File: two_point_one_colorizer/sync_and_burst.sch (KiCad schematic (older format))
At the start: 12 parts, among them J5 Conn_01x03, U4 LM1881, U5 74HC86, U6 4013

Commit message: update circuits
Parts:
- added R?: 1.5k, Resistor_THT:R_Axial_DIN0207_L6.3mm_D2.5mm_P7.62mm_Horizontal, symbol Device:R
- R10: value 10k -> 1k
- R14: value 12k -> 1.5k
- R9: value 1k -> 10k
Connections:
- net GND: now also R?.1; no longer R10.1
- new net black_and_sync: R10.1, R?.2
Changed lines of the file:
@@
 P 9200 5325
 F 0 "R14" H 9270 5371 50  0000 L CNN
-F 1 "12k" H 9270 5280 50  0000 L CNN
+F 1 "1.5k" H 9270 5280 50  0000 L CNN
 F 2 "Resistor_THT:R_Axial_DIN0207_L6.3mm_D2.5mm_P7.62mm_Horizontal" V 9130 5325 50  0001 C CNN
 F 3 "~" H 9200 5325 50  0001 C CNN
@@
 P 6075 1500
 F 0 "R9" H 5950 1500 50  0000 C CNN
-F 1 "1k" H 5900 1600 50  0000 C CNN
+F 1 "10k" H 5900 1600 50  0000 C CNN
 F 2 "Resistor_THT:R_Axial_DIN0207_L6.3mm_D2.5mm_P7.62mm_Horizontal" V 6005 1500 50  0001 C CNN
 F 3 "~" H 6075 1500 50  0001 C CNN
@@
 P 6575 1800
 F 0 "R10" V 6368 1800 50  0000 C CNN
-F 1 "10k" V 6459 1800 50  0000 C CNN
+F 1 "1k" V 6459 1800 50  0000 C CNN
 F 2 "Resistor_THT:R_Axial_DIN0207_L6.3mm_D2.5mm_P7.62mm_Horizontal" V 6505 1800 50  0001 C CNN
 F 3 "~" H 6575 1800 50  0001 C CNN
@@
 L power:GND #PWR?
 U 1 1 5F2CD17D
-P 6800 1950
+P 7225 1950
 AR Path="/5F2CD17D" Ref="#PWR?"  Part="1"
 AR Path="/5F1CF562/5F2CD17D" Ref="#PWR030"  Part="1"
-F 0 "#PWR030" H 6800 1700 50  0001 C CNN
-F 1 "GND" H 6805 1777 50  0000 C CNN
-F 2 "" H 6800 1950 50  0001 C CNN
-F 3 "" H 6800 1950 50  0001 C CNN
-	1    6800 1950
+F 0 "#PWR030" H 7225 1700 50  0001 C CNN
+F 1 "GND" H 7230 1777 50  0000 C CNN
+F 2 "" H 7225 1950 50  0001 C CNN
+F 3 "" H 7225 1950 50  0001 C CNN
+	1    7225 1950
 	1    0    0    -1
 $EndComp
@@
 	5025 1800 6075 1800
 Connection ~ 6075 1800
+$Comp
+L Device:R R?
+U 1 1 5F549749
+P 6950 1950
+F 0 "R?" V 6850 1950 50  0000 C CNN
+F 1 "1.5k" V 7050 1950 50  0000 C CNN
+F 2 "Resistor_THT:R_Axial_DIN0207_L6.3mm_D2.5mm_P7.62mm_Horizontal" V 6880 1950 50  0001 C CNN
+F 3 "~" H 6950 1950 50  0001 C CNN
+	1    6950 1950
+	0    1    1    0
+$EndComp
+Wire Wire Line
+	7225 1950 7100 1950
 $EndSCHEMATC

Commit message: revised all boards
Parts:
- U6: value 4013 -> CD4013
- gave numbers to parts that had none: 1
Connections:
- net at U6.3 (C): now also R10.2, R9.1, U4.1 (CSYNC); no longer U4.3 (FRAME)
- no-connect marks 7 -> 8
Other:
- note added: "csync"
- note removed: "vsync"
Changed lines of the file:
@@
 P 4675 5525
 F 0 "U6" H 4900 6000 50  0000 C CNN
-F 1 "4013" H 4900 5900 50  0000 C CNN
+F 1 "CD4013" H 4900 5900 50  0000 C CNN
 F 2 "Package_DIP:DIP-14_W7.62mm_LongPads" H 4675 5525 50  0001 C CNN
 F 3 "http://www.onsemi.com/pub/Collateral/MC14013B-D.PDF" H 4675 5525 50  0001 C CNN
@@
 P 2200 7100
 F 0 "U6" H 2430 7146 50  0000 L CNN
-F 1 "4013" H 2430 7055 50  0000 L CNN
+F 1 "CD4013" H 2430 7055 50  0000 L CNN
 F 2 "Package_DIP:DIP-14_W7.62mm_LongPads" H 2200 7100 50  0001 C CNN
 F 3 "http://www.onsemi.com/pub/Collateral/MC14013B-D.PDF" H 2200 7100 50  0001 C CNN
@@
 	5075 4950 5075 5625
 Text Notes 3975 5450 0    50   ~ 0
-vsync
+csync
 $Comp
 L 4xxx:4013 U6
@@
 P 3325 7125
 F 0 "U6" H 3325 7606 50  0000 C CNN
-F 1 "4013" H 3325 7515 50  0000 C CNN
+F 1 "CD4013" H 3325 7515 50  0000 C CNN
 F 2 "Package_DIP:DIP-14_W7.62mm_LongPads" H 3325 7125 50  0001 C CNN
 F 3 "http://www.onsemi.com/pub/Collateral/MC14013B-D.PDF" H 3325 7125 50  0001 C CNN
@@
 	3725 3500 5400 3500
 Wire Wire Line
-	5400 3500 5400 2125
-Wire Wire Line
-	5400 2125 5025 2125
-Wire Wire Line
 	5025 2225 7650 2225
 Wire Wire Line
@@
 Connection ~ 6075 1800
 $Comp
-L Device:R R?
+L Device:R R35
 U 1 1 5F549749
 P 6950 1950
-F 0 "R?" V 6850 1950 50  0000 C CNN
+F 0 "R35" V 6850 1950 50  0000 C CNN
 F 1 "1.5k" V 7050 1950 50  0000 C CNN
 F 2 "Resistor_THT:R_Axial_DIN0207_L6.3mm_D2.5mm_P7.62mm_Horizontal" V 6880 1950 50  0001 C CNN
@@
 Wire Wire Line
 	7225 1950 7100 1950
+Wire Wire Line
+	5400 2025 5025 2025
+Wire Wire Line
+	5400 2025 5400 3500
+Connection ~ 5025 2025
+NoConn ~ 5025 2125
 $EndSCHEMATC

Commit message: working on nexr version for colorizer and inverter
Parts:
- removed J5: Conn_01x03, Connector_PinHeader_2.54mm:PinHeader_1x03_P2.54mm_Vertical, symbol Connector_Generic:Conn_01x03
- added C21: 0.1n, Capacitor_THT:C_Disc_D4.7mm_W2.5mm_P5.00mm, symbol Device:C_Small
- added R36: 10k, Resistor_THT:R_Axial_DIN0207_L6.3mm_D2.5mm_P7.62mm_Horizontal, symbol Device:R
- added RV9: 20k_pot, lib_fp:Potentiometer_Vertical_Large, symbol Device:R_POT
- added SW4: SPDT_slide, lib_fp:spdt_slide_switch_small_tayda, symbol Switch:SW_SPDT
- added U11: 74HC4538, Package_DIP:DIP-16_W7.62mm_LongPads, symbol symbol:74HC4538
- R35: value 1.5k -> 1k (or 1.2k maybe)
- U4: footprint Package_DIP:DIP-8_W7.62mm_LongPads -> lib_fp:DIP-SOIC-8
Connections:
- net +5V: now also R9.1, RV9.1, U11.16 (VDD), U11.3 (~CD); no longer R9.2, U6.6 (S)
- net GND: now also U6.6 (S), SW4.1 (A), U11.4 (B), U11.8 (VSS)
- net burst_pulse: now also U11.7 (~Q); no longer U4.5 (BURST)
- net at U6.1 (Q): now also SW4.3 (C)
- net at R10.2, U4.1 (CSYNC), U6.3 (C): now also R9.2, U11.5 (~A); no longer R9.1
- net at U5.10: now also SW4.2 (B)
- new net: C21.2, U11.1 (Cx)
- new net: C21.1, R36.2, U11.2 (RxCx)
- new net: R36.1, RV9.2
- no-connect marks 8 -> 18
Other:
- moved on the sheet: C12, C13, R10, R11, R12, R13, R14, R35, R9, U4, U5C, U6A

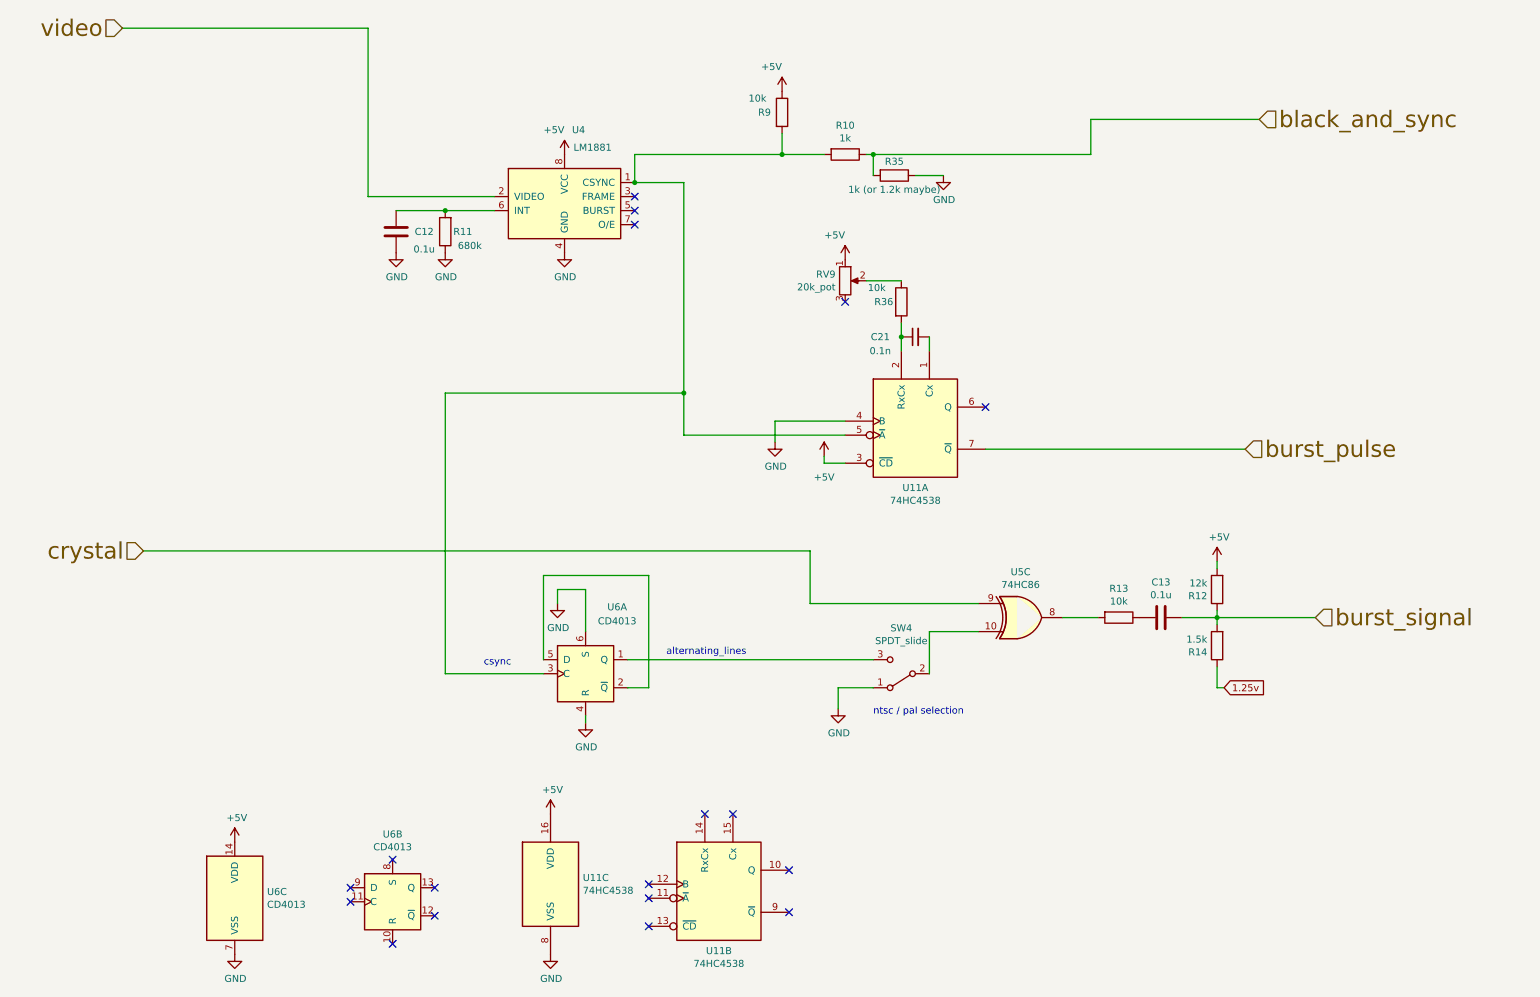
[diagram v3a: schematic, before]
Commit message: lay out colorizer
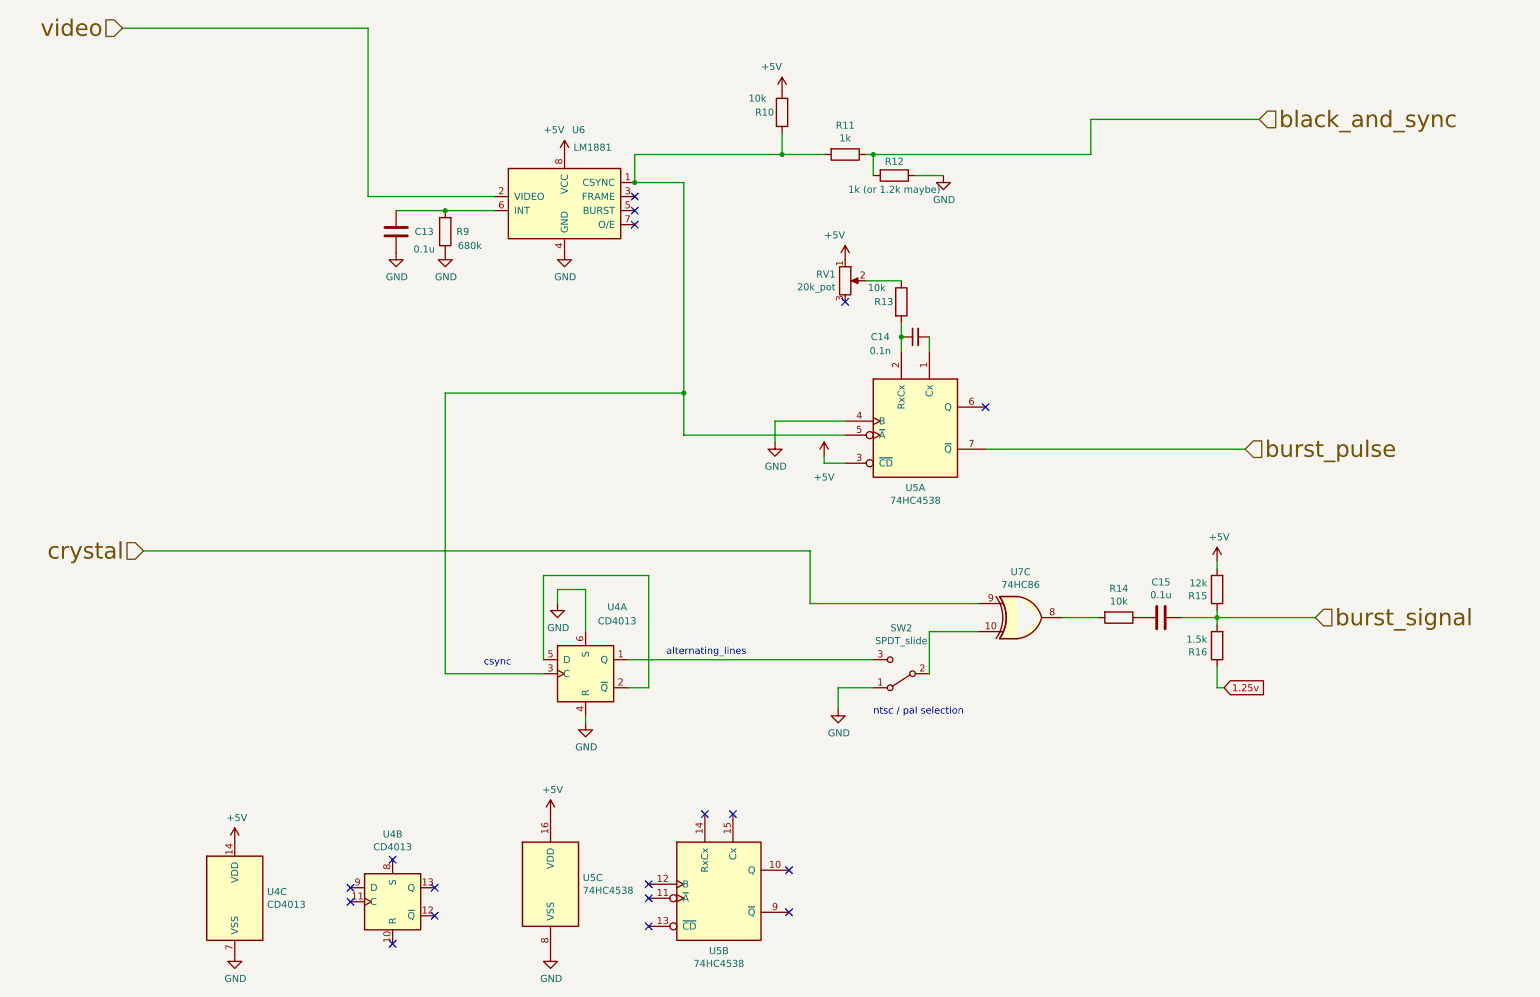
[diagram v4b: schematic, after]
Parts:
- C13: renamed from C12; footprint Capacitor_THT:C_Disc_D4.7mm_W2.5mm_P5.00mm -> lib_fp:C_Disc_D4.7mm_W2.5mm_P5.00mm
- C14: renamed from C21; footprint Capacitor_THT:C_Disc_D4.7mm_W2.5mm_P5.00mm -> lib_fp:C_Disc_D4.7mm_W2.5mm_P5.00mm
- C15: renamed from C13; footprint Capacitor_THT:C_Disc_D4.7mm_W2.5mm_P5.00mm -> lib_fp:C_Disc_D4.7mm_W2.5mm_P5.00mm
- R10: renamed from R9; footprint Resistor_THT:R_Axial_DIN0207_L6.3mm_D2.5mm_P7.62mm_Horizontal -> lib_fp:R_Axial_DIN0207_L6.3mm_D2.5mm_P7.62mm_Horizontal
- R11: renamed from R10; footprint Resistor_THT:R_Axial_DIN0207_L6.3mm_D2.5mm_P7.62mm_Horizontal -> lib_fp:R_Axial_DIN0207_L6.3mm_D2.5mm_P7.62mm_Horizontal
- R12: renamed from R35; footprint Resistor_THT:R_Axial_DIN0207_L6.3mm_D2.5mm_P7.62mm_Horizontal -> lib_fp:R_Axial_DIN0207_L6.3mm_D2.5mm_P7.62mm_Horizontal
- R13: renamed from R36; footprint Resistor_THT:R_Axial_DIN0207_L6.3mm_D2.5mm_P7.62mm_Horizontal -> lib_fp:R_Axial_DIN0207_L6.3mm_D2.5mm_P7.62mm_Horizontal
- R14: renamed from R13; footprint Resistor_THT:R_Axial_DIN0207_L6.3mm_D2.5mm_P7.62mm_Horizontal -> lib_fp:R_Axial_DIN0207_L6.3mm_D2.5mm_P7.62mm_Horizontal
- R15: renamed from R12; footprint Resistor_THT:R_Axial_DIN0207_L6.3mm_D2.5mm_P7.62mm_Horizontal -> lib_fp:R_Axial_DIN0207_L6.3mm_D2.5mm_P7.62mm_Horizontal
- R16: renamed from R14; footprint Resistor_THT:R_Axial_DIN0207_L6.3mm_D2.5mm_P7.62mm_Horizontal -> lib_fp:R_Axial_DIN0207_L6.3mm_D2.5mm_P7.62mm_Horizontal
- R9: renamed from R11; footprint Resistor_THT:R_Axial_DIN0207_L6.3mm_D2.5mm_P7.62mm_Horizontal -> lib_fp:R_Axial_DIN0207_L6.3mm_D2.5mm_P7.62mm_Horizontal
- renumbered RV9 to RV1, SW4 to SW2, U6 to U4, U11 to U5, U4 to U6, U5 to U7
